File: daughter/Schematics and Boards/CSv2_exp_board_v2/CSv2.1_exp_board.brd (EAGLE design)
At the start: 38.1 x 47 mm, 103 parts, among them J1 HIROSE-DF40_50-PIN_CONNECTORS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, J3 CORTEX_DEBUG_SMD, J4 SJ-43514-SMTC, J6 ATTINY_AVR_DEBUG, J7 J-USB-HIROSE-MICRO-USB, SW1 SPST_TACT-KMR2, SW2 SPST_TACT-KMR2, U1 LOADSWITCH-MIC94164, U10 LOADSWITCH-MIC94164, U11 BMI160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

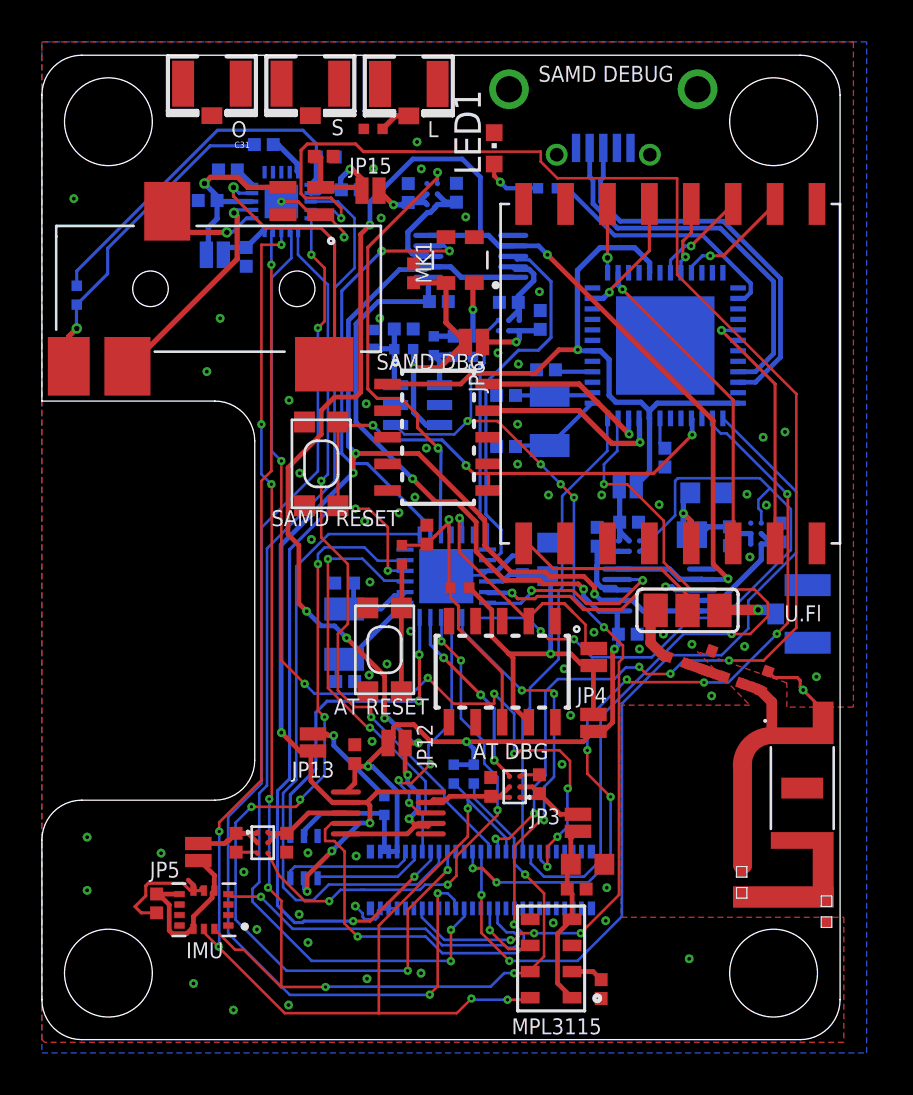
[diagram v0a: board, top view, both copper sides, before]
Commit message: Fixed all clearance issues for increased min trace/space/via sizes
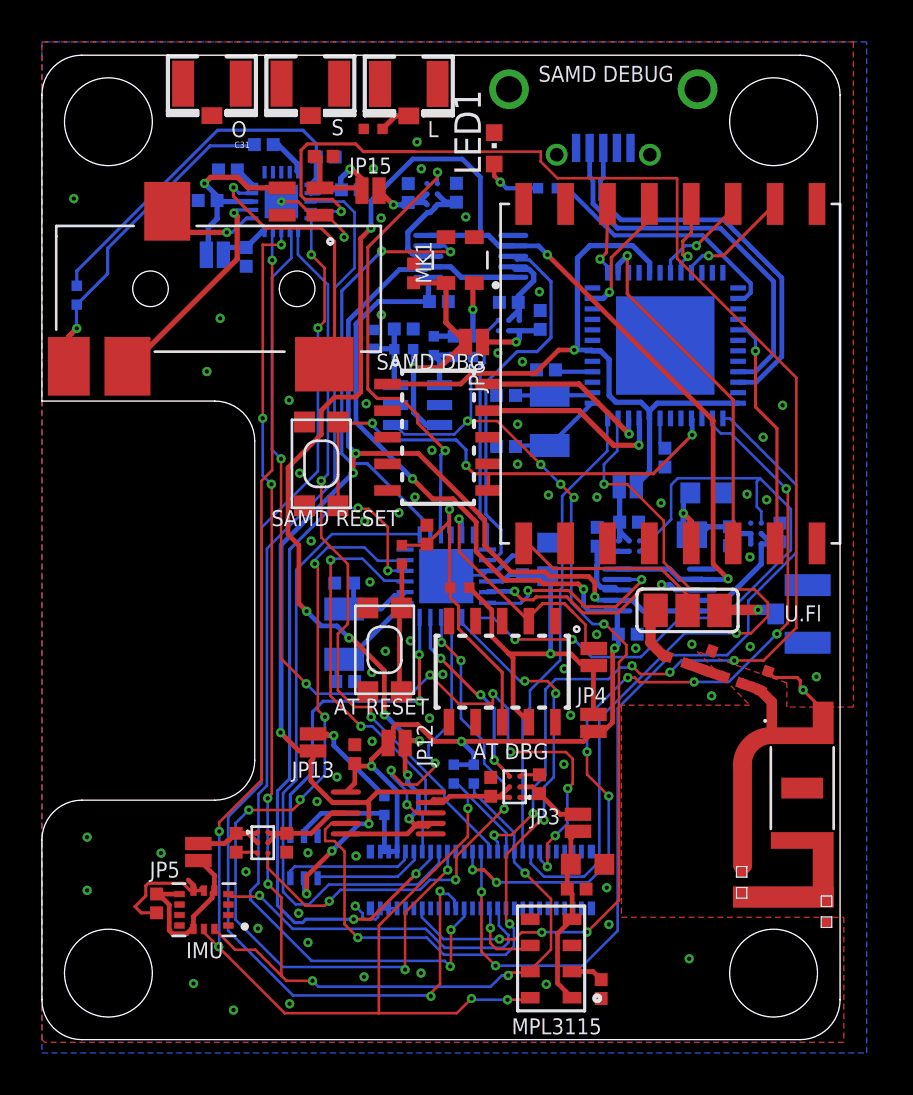
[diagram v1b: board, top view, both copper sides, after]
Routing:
- net MEAS_BARO: track 12.0 -> 13.8 mm
- net LORA_IRQ0: track 15.2 -> 16.8 mm
- net AT_RESET: track 14.4 -> 15.8 mm
- net DTR_BUS1_P2: track 42.1 -> 43.5 mm
- net DTR_BUS2_GPIO1: track 17.3 -> 16.5 mm
- net LORA_IRQ1: track 12.0 -> 11.2 mm
- net EN_IMU: track 24.9 -> 25.7 mm
- net DTR_BUS1_GPIO2/AIN0: track 44.9 -> 45.7 mm
- net DTR_BUS0_GPIO1/I2S_MCK: track 50.5 -> 51.1 mm
- net GND: vias 66 -> 69

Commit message: DTR: fixed all airwires
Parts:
- moved U16 2.89 mm to (10.4, 42.1)
- moved C42 0.61 mm to (12.8, 42.2), turned to 270 degrees
- moved C45 0.24 mm to (28.0, 19.6)
- moved C40 0.22 mm to (25.8, 8.37)
- moved JP4 0.20 mm to (26.1, 15.1)
- moved C35 0.17 mm to (14.6, 40.6)
- moved JP14 0.07 mm to (26.3, 18.2)
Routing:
- net DTR_BUS0_P2/I2S_FS0: track 71.8 -> 67.9 mm
- net GND: track 38.8 -> 35.8 mm, vias 69 -> 75
- net +1V8_CODEC: track 9.59 -> 8.20 mm
- net MEAS_IMU: track 34.7 -> 35.6 mm
- net EN_RADIO: track 32.6 -> 33.3 mm
- net +3V3_DTR: track 63.1 -> 63.8 mm

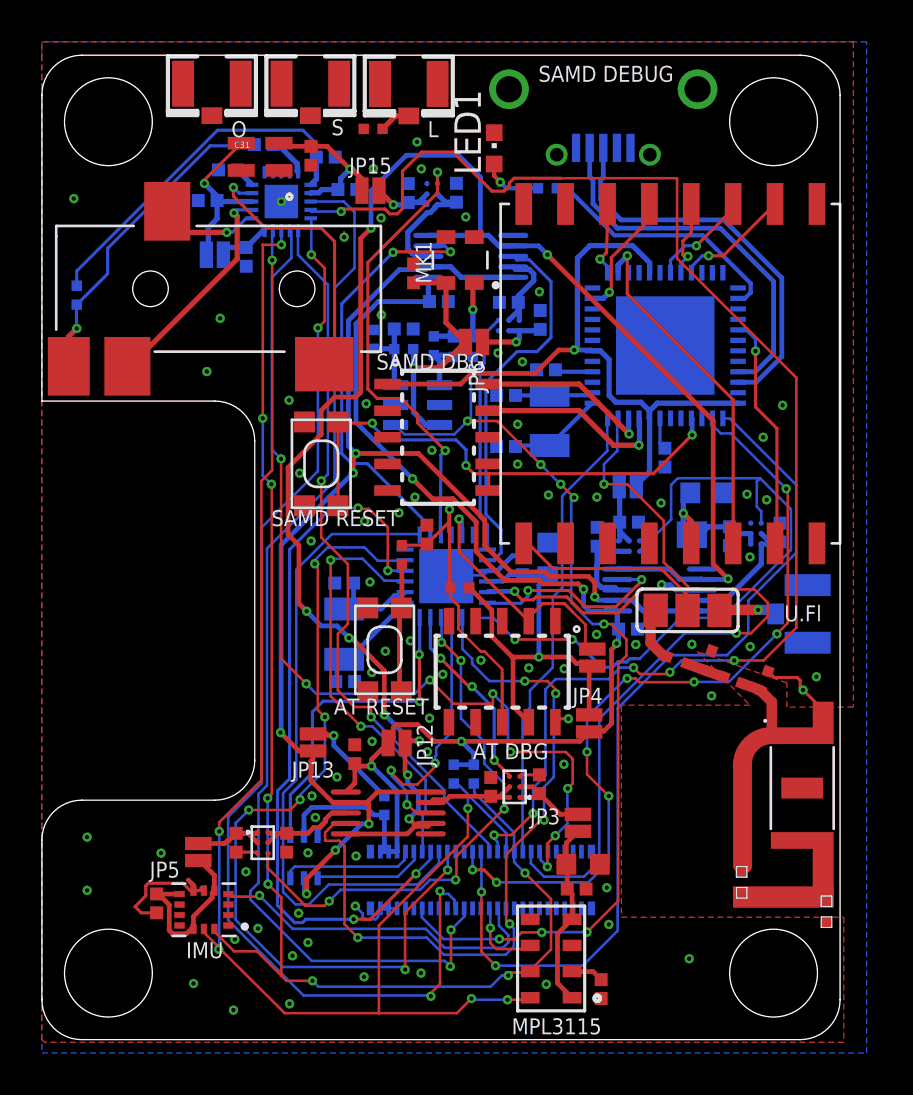
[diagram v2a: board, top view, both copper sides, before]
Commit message: DTR - fixed BOM
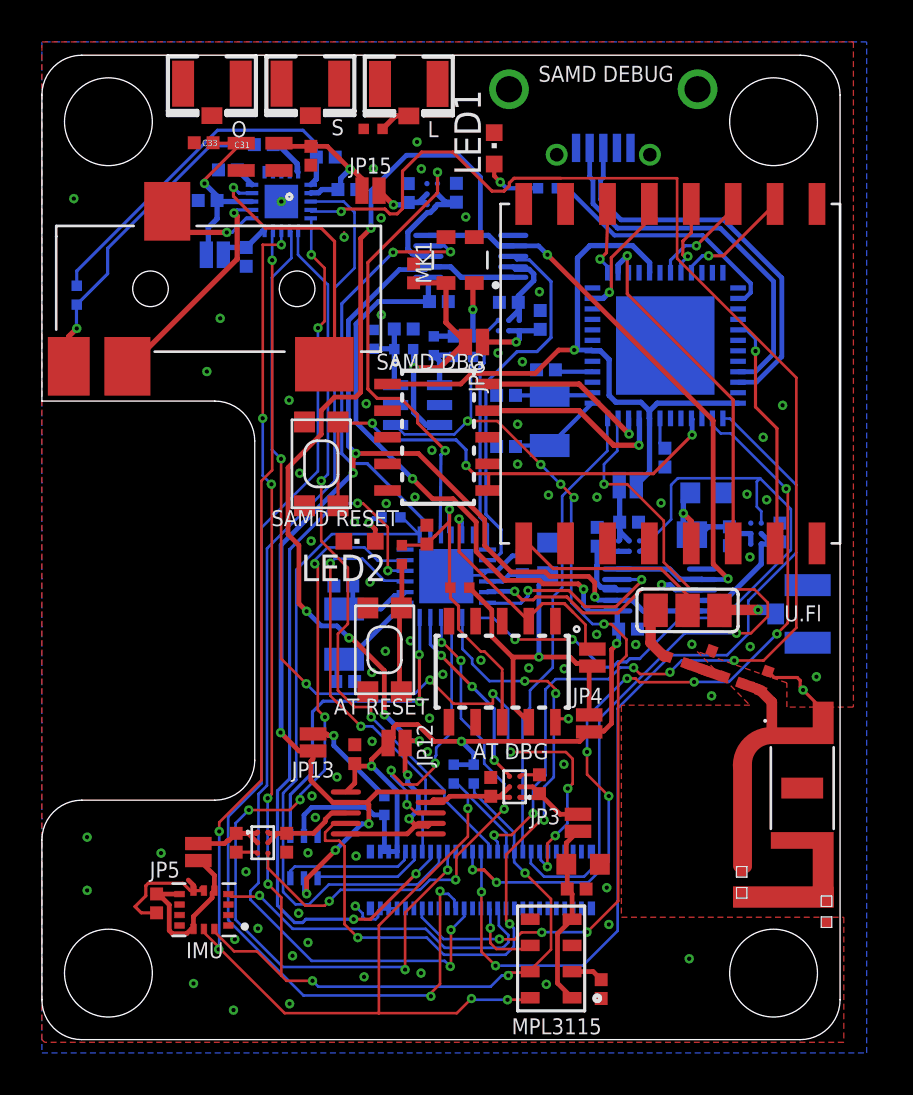
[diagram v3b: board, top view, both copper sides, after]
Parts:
- added C33: 0.1u, Capacitors:C0402
- added LED2: (no value), Diodes:CHIPLED_0603
- added R12: 1k, Resistors:R0402
- R11: value (none) -> 1k
- R30: value 1.2n -> 0R
- R8: value (none) -> 0R
- moved C16 0.14 mm to (14.4, 21.7)
- renumbered L1 to R30
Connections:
- net IN+ renamed N$3
- new net DTR_DETECT_LED: LED2.A, R12.2
- net +1V8_CODEC: now also C33.1
- net DTR_DETECT: now also R12.1
- net GND: now also C33.2, LED2.C
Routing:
- net DTR_DETECT_LED: track 0.00 -> 1.72 mm, vias 0 -> 1
- net +1V8_CODEC: track 8.20 -> 9.55 mm
- net DTR_DETECT: track 31.3 -> 32.6 mm

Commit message: DTR-fixed silk screem and switched to a new pressure sensor
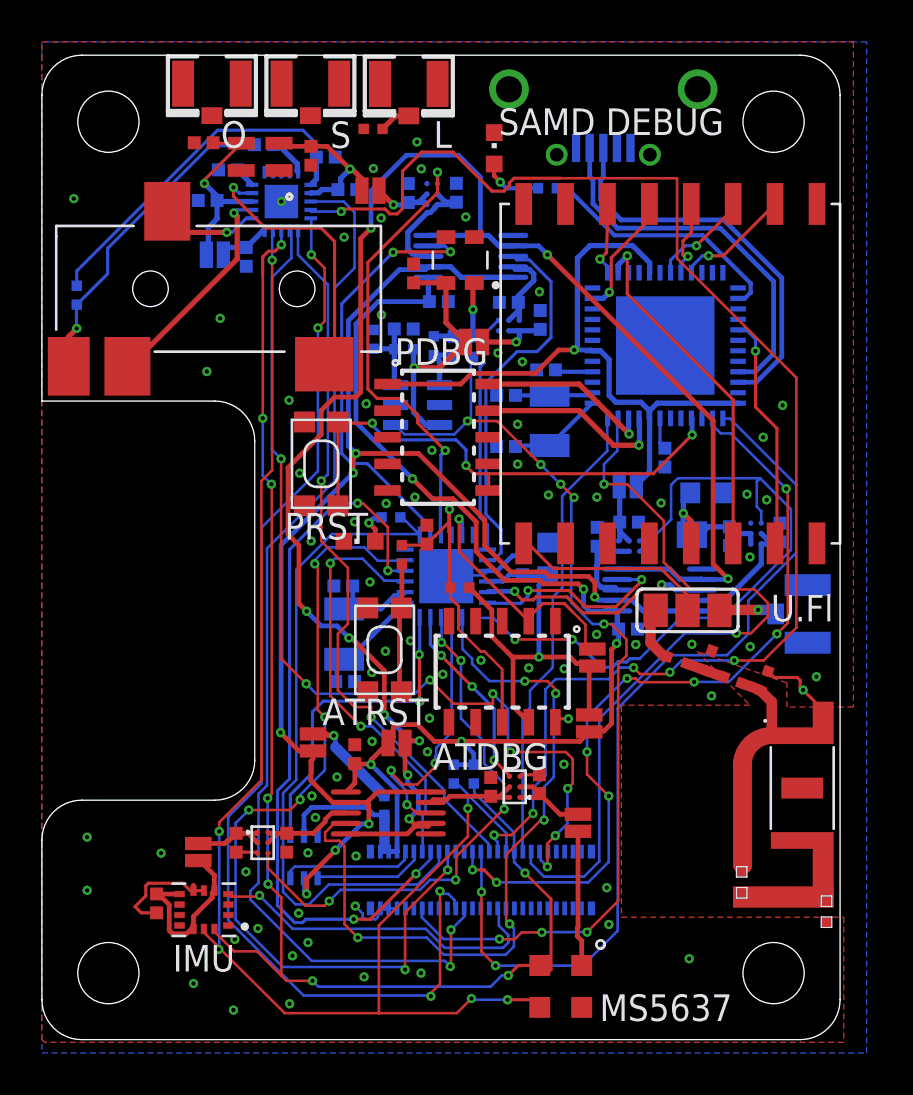
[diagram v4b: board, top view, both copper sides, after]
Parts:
- removed C40: 10u, Capacitors:C0603
- removed C47, C48: 0.1u, Capacitors:C0402
- removed U18: MPL3115A2, Sensors:MPL3115A2_PSON125P300X500X120-8N
- added U206: MS5637, Sensors:MS5637
- renumbered LED1 to RED_LED, LED2 to GREEN_LED
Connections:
- removed net N$10: C48.1, U18.2
- net +3V3_BARO: now also U206.1; no longer C40.2, C47.1, U18.1, U18.4
- net DTR_BUS2_GPIO0: no longer U18.6
- net DTR_BUS2_P0/I2C_SDA: now also U206.2; no longer U18.7
- net DTR_BUS2_P1/I2C_SCL: now also U206.3; no longer U18.8
- net GND: now also U206.4; no longer C40.1, C47.2, C48.2, U18.3
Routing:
- net DTR_BUS2_GPIO0: track 3.83 -> 0.07 mm, vias 1 -> 0
- net +3V3_BARO: track 8.87 -> 6.51 mm
- net N$10: track 1.55 -> 0.00 mm
- net GND: track 35.9 -> 35.1 mm, vias 75 -> 74
- net DTR_BUS2_P1/I2C_SCL: track 69.7 -> 70.3 mm
- net DTR_BUS2_P0/I2C_SDA: track 64.5 -> 65.0 mm
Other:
- board text added: "ATDBG"
- board text added: "ATRST"
- board text added: "ATTINY"
- board text added: "CS Daughter Card v2 Eve Hu 9/12/2020"
- board text added: "MS5637"
- board text added: "PDBG"
- board text added: "PRST"
- board text removed: "AT DBG"
- board text removed: "AT RESET"
- board text removed: "ATTINY817"
- board text removed: "CommonSense Daughter Board v1 Eve Hu 7/2/2020"
- board text removed: "MPL3115"
- board text removed: "SAMD DBG"
- board text removed: "SAMD RESET"
